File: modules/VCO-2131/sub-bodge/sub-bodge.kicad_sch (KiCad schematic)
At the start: 2 parts

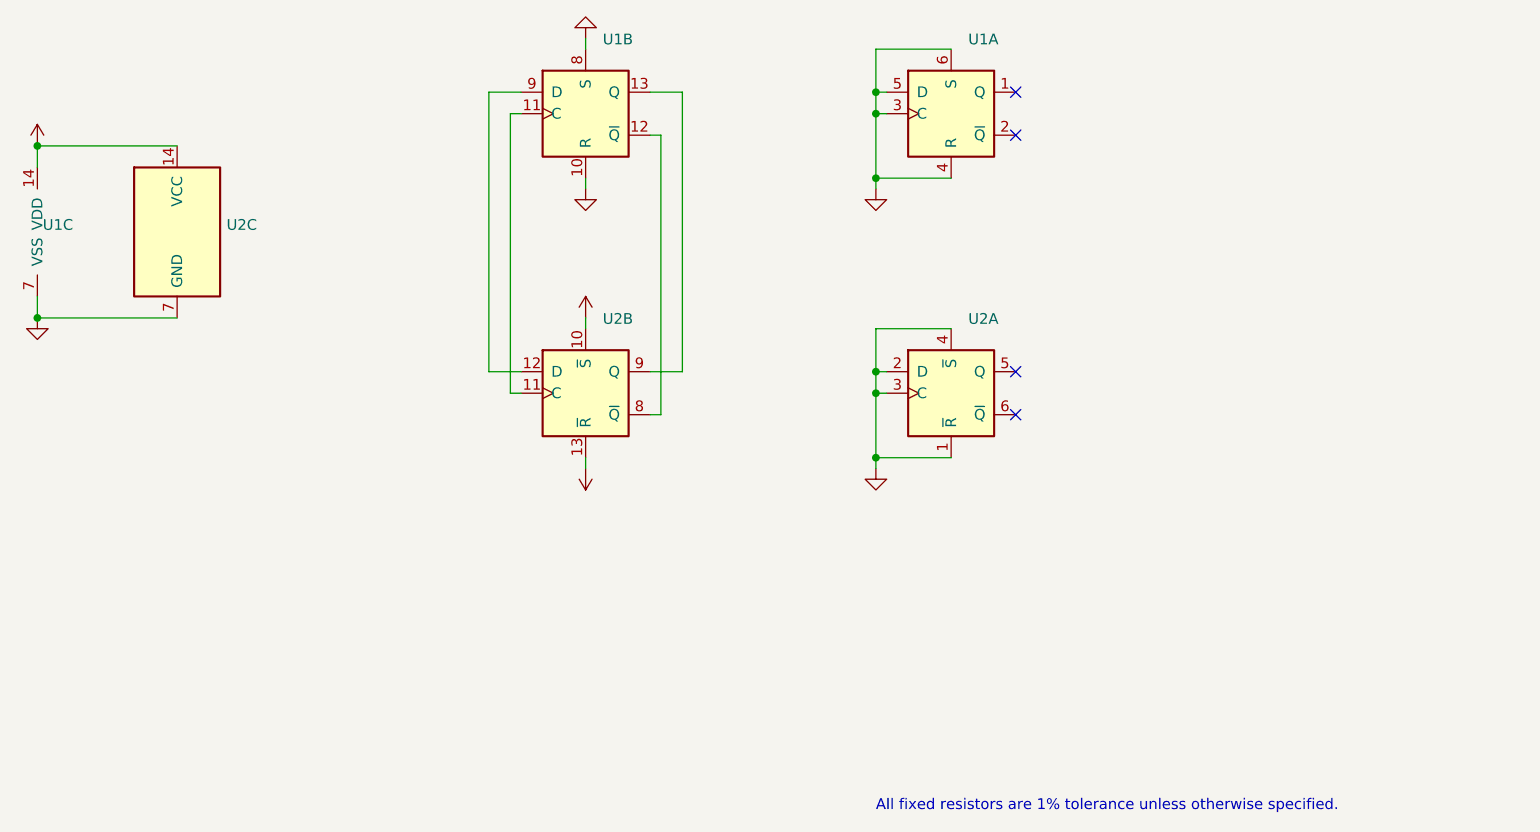
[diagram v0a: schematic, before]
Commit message: VCO sub fix - PCB with SOIC
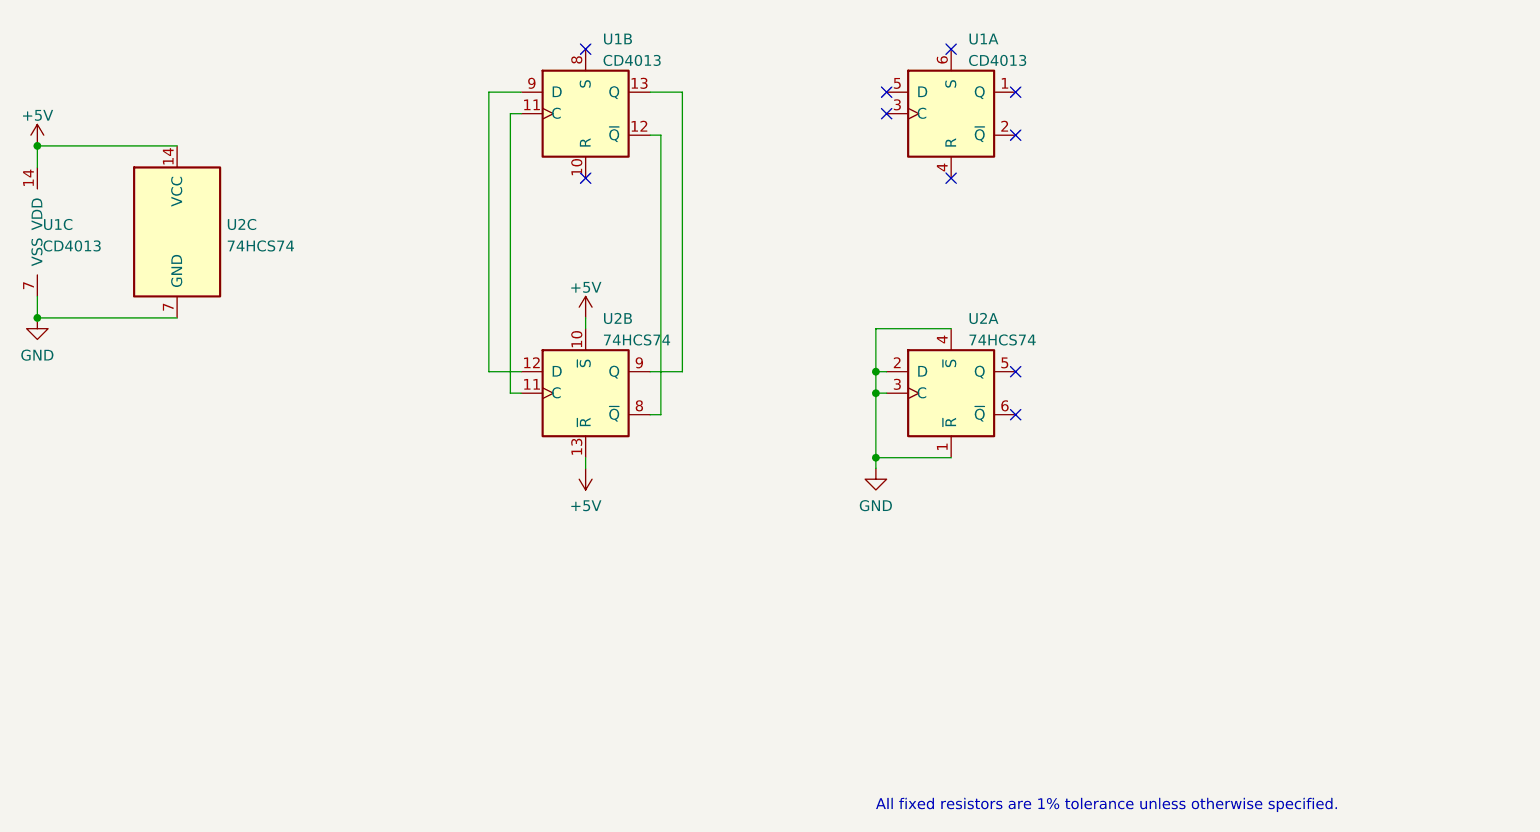
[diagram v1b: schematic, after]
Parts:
- U1: value (none) -> CD4013; footprint (none) -> Package_DIP:DIP-14_W7.62mm
- U2: value (none) -> 74HCS74; footprint (none) -> Package_SO:SOIC-14_3.9x8.7mm_P1.27mm
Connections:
- net GND: no longer U1.10 (R), U1.3 (C), U1.4 (R), U1.5 (D), U1.6 (S), U1.8 (S)
- no-connect marks 4 -> 10

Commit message: VCO sub fix - PCB with SOIC
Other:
- title: [title] -> VCO-2131 Sub Bodge
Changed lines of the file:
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@@
   (paper "A4")
   (title_block
-    (title "[title]")
-    (rev "0.1")
+    (title "VCO-2131 Sub Bodge")
+    (date "2022-07-04")
+    (rev "1.0")
     (company "Len Popp")
     (comment 1 "Copyright © 2022 Len Popp CC BY")
-    (comment 2 "[description]")
+    (comment 2 "Bodge board to fix sub-oscillator")
   )
   (junction (at 177.8 104.14) (diameter 0) (color 0 0 0 0)

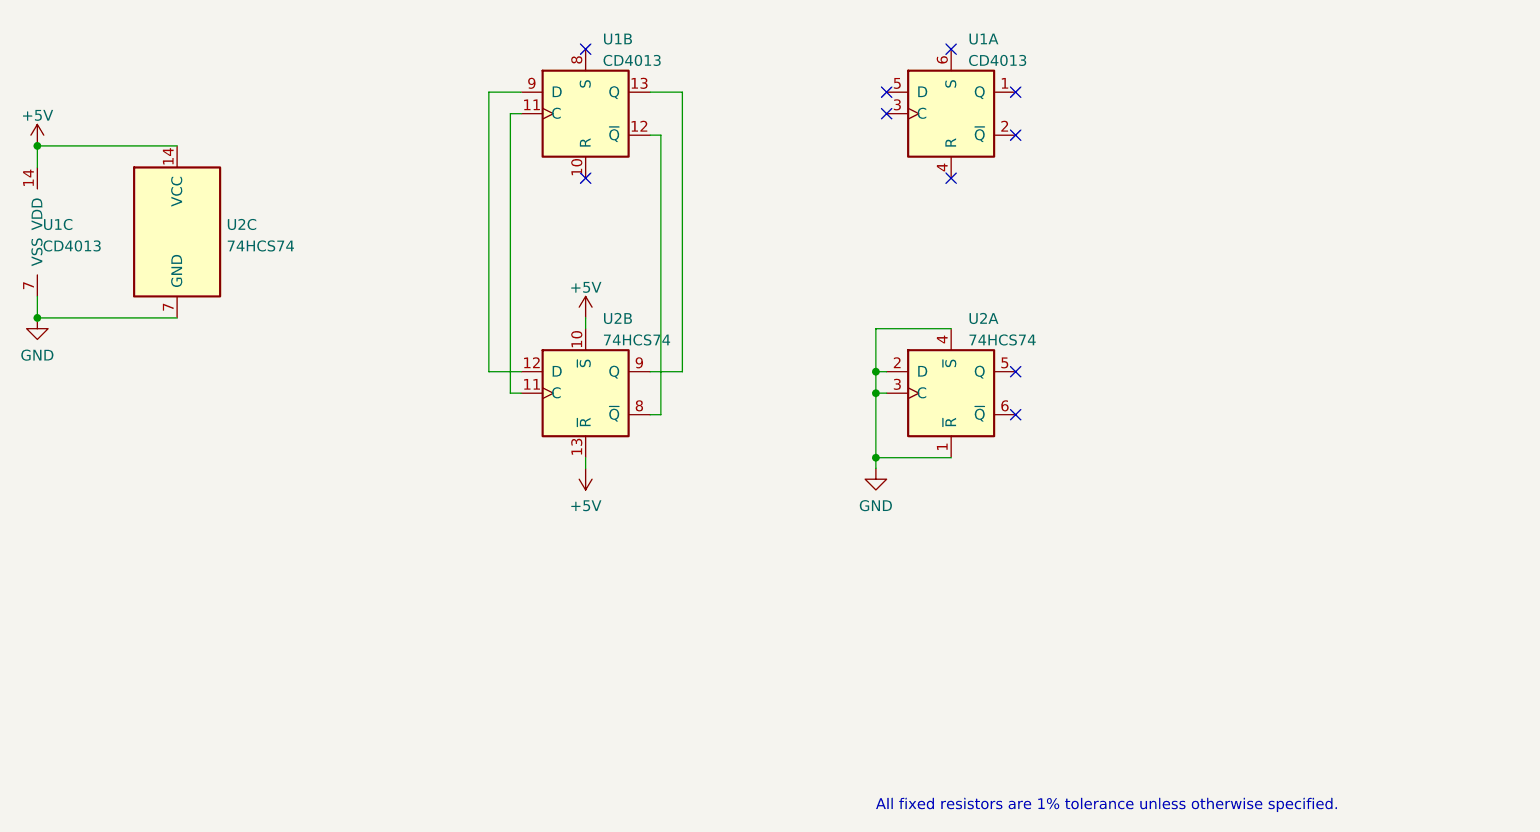
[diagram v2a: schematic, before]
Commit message: VCO sub fix - update component
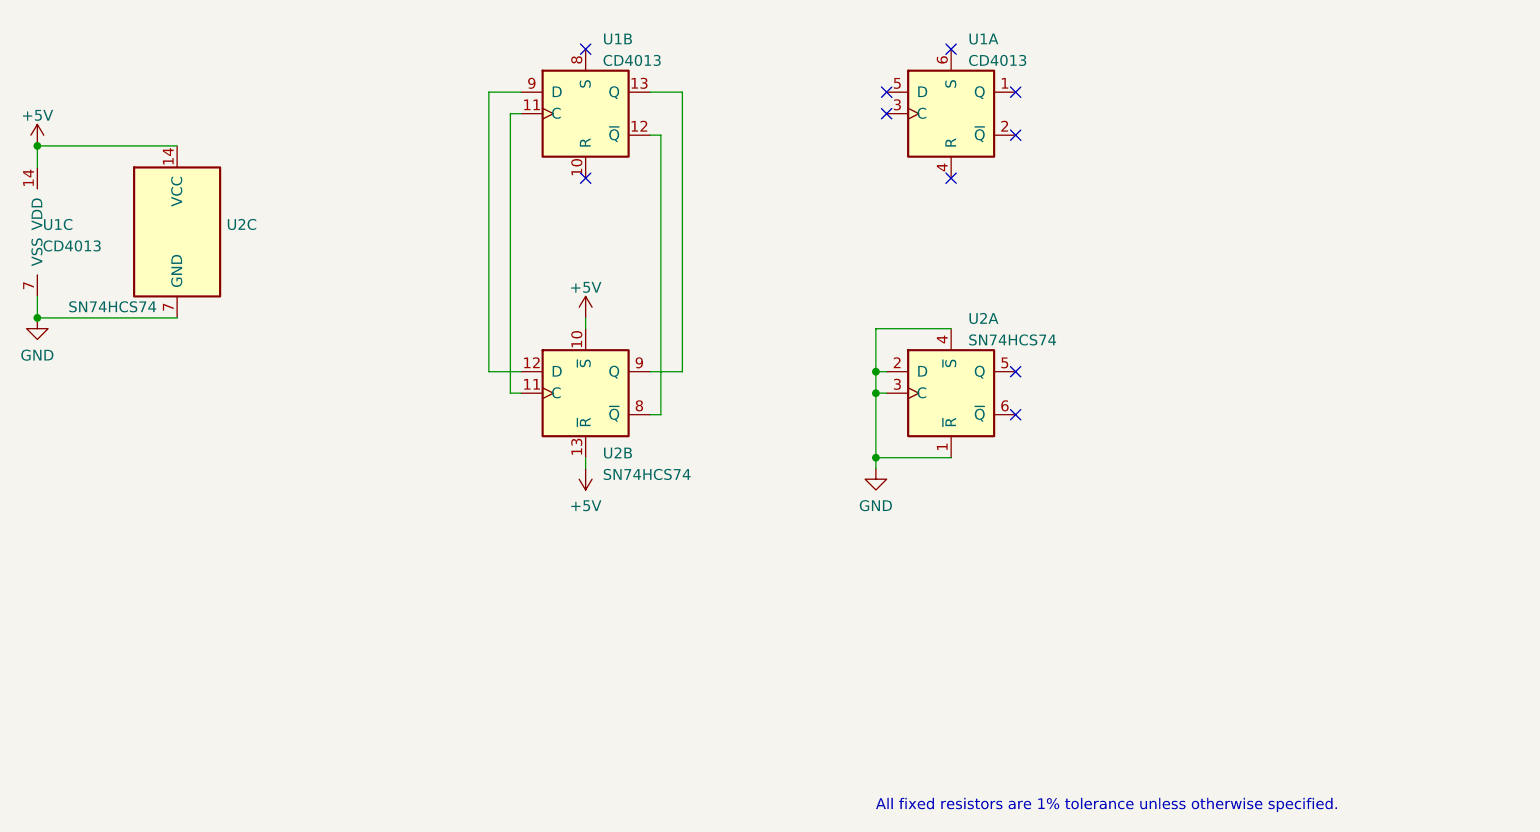
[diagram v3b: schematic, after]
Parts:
- U2: value 74HCS74 -> SN74HCS74; symbol 74xx:74HC74 -> -lmp-IC-misc:SN74HCS74; Distributor (none) -> Mouser; DistributorPartLink (none) -> https://www.mouser.ca/ProductDetail/Texas-Instruments/SN74H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; DistributorPartNum (none) -> 595-SN74HCS74DR; Manufacturer (none) -> Texas Instruments; ManufacturerPartNum (none) -> SN74HCS74DR
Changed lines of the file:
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@@
     (pin "7")
   )
-  (symbol (lib_id "74xx:74HC74") (at 95.25 87.63 0) (unit 3)
+  (symbol (lib_id "-lmp-IC-misc:SN74HCS74") (at 95.25 87.63 0) (unit 3)
     (in_bom yes) (on_board yes) (fields_autoplaced)
     (property "Reference" "U2" (id 0) (at 101.092 86.7953 0)
       (effects (font (size 1.27 1.27)) (justify left))
     )
-    (property "Value" "74HCS74" (id 1) (at 101.092 89.3322 0)
-      (effects (font (size 1.27 1.27)) (justify left))
-    )
+    (property "Value" "SN74HCS74" (id 1) (at 87.63 96.52 0))
     (property "Footprint" "Package_SO:SOIC-14_3.9x8.7mm_P1.27mm" (id 2) (at 95.25 87.63 0)
       (effects (font (size 1.27 1.27)) hide)
     )
     (property "Datasheet" "https://www.ti.com/lit/ds/symlink/sn74hcs74.pdf" (id 3) (at 95.25 87.63 0)
+      (effects (font (size 1.27 1.27)) hide)
+    )
+    (property "Manufacturer" "Texas Instruments" (id 4) (at 95.25 87.63 0)
+      (effects (font (size 1.27 1.27)) hide)
+    )
+    (property "ManufacturerPartNum" "SN74HCS74DR" (id 5) (at 95.25 87.63 0)
+      (effects (font (size 1.27 1.27)) hide)
+    )
+    (property "Distributor" "Mouser" (id 6) (at 95.25 87.63 0)
+      (effects (font (size 1.27 1.27)) hide)
+    )
+    (property "DistributorPartNum" "595-SN74HCS74DR" (id 7) (at 95.25 87.63 0)
+      (effects (font (size 1.27 1.27)) hide)
+    )
+    (property "DistributorPartLink" "https://www.mouser.ca/ProductDetail/Texas-Instruments/SN74HCS74DR?qs=TiOZkKH1s2QvGxo75w4r5Q%3D%3D" (id 8) (at 95.25 87.63 0)
       (effects (font (size 1.27 1.27)) hide)
     )
@@
     (pin "1")
   )
-  (symbol (lib_id "74xx:74HC74") (at 143.51 106.68 0) (unit 2)
-    (in_bom yes) (on_board yes) (fields_autoplaced)
-    (property "Reference" "U2" (id 0) (at 145.5294 97.9002 0)
-      (effects (font (size 1.27 1.27)) (justify left))
-    )
-    (property "Value" "74HCS74" (id 1) (at 145.5294 100.4371 0)
+  (symbol (lib_id "-lmp-IC-misc:SN74HCS74") (at 143.51 106.68 0) (unit 2)
+    (in_bom yes) (on_board yes) (fields_autoplaced)
+    (property "Reference" "U2" (id 0) (at 145.5294 113.7904 0)
+      (effects (font (size 1.27 1.27)) (justify left))
+    )
+    (property "Value" "SN74HCS74" (id 1) (at 145.5294 116.3273 0)
       (effects (font (size 1.27 1.27)) (justify left))
     )
@@
     )
     (property "Datasheet" "https://www.ti.com/lit/ds/symlink/sn74hcs74.pdf" (id 3) (at 143.51 106.68 0)
+      (effects (font (size 1.27 1.27)) hide)
+    )
+    (property "Manufacturer" "Texas Instruments" (id 4) (at 143.51 106.68 0)
+      (effects (font (size 1.27 1.27)) hide)
+    )
+    (property "ManufacturerPartNum" "SN74HCS74DR" (id 5) (at 143.51 106.68 0)
+      (effects (font (size 1.27 1.27)) hide)
+    )
+    (property "Distributor" "Mouser" (id 6) (at 143.51 106.68 0)
+      (effects (font (size 1.27 1.27)) hide)
+    )
+    (property "DistributorPartNum" "595-SN74HCS74DR" (id 7) (at 143.51 106.68 0)
+      (effects (font (size 1.27 1.27)) hide)
+    )
+    (property "DistributorPartLink" "https://www.mouser.ca/ProductDetail/Texas-Instruments/SN74HCS74DR?qs=TiOZkKH1s2QvGxo75w4r5Q%3D%3D" (id 8) (at 143.51 106.68 0)
       (effects (font (size 1.27 1.27)) hide)
     )
@@
     (pin "1")
   )
-  (symbol (lib_id "74xx:74HC74") (at 186.69 106.68 0) (unit 1)
+  (symbol (lib_id "-lmp-IC-misc:SN74HCS74") (at 186.69 106.68 0) (unit 1)
     (in_bom yes) (on_board yes) (fields_autoplaced)
     (property "Reference" "U2" (id 0) (at 188.7094 97.9002 0)
       (effects (font (size 1.27 1.27)) (justify left))
     )
-    (property "Value" "74HCS74" (id 1) (at 188.7094 100.4371 0)
+    (property "Value" "SN74HCS74" (id 1) (at 188.7094 100.4371 0)
       (effects (font (size 1.27 1.27)) (justify left))
     )
@@
     )
     (property "Datasheet" "https://www.ti.com/lit/ds/symlink/sn74hcs74.pdf" (id 3) (at 186.69 106.68 0)
+      (effects (font (size 1.27 1.27)) hide)
+    )
+    (property "Manufacturer" "Texas Instruments" (id 4) (at 186.69 106.68 0)
+      (effects (font (size 1.27 1.27)) hide)
+    )
+    (property "ManufacturerPartNum" "SN74HCS74DR" (id 5) (at 186.69 106.68 0)
+      (effects (font (size 1.27 1.27)) hide)
+    )
+    (property "Distributor" "Mouser" (id 6) (at 186.69 106.68 0)
+      (effects (font (size 1.27 1.27)) hide)
+    )
+    (property "DistributorPartNum" "595-SN74HCS74DR" (id 7) (at 186.69 106.68 0)
+      (effects (font (size 1.27 1.27)) hide)
+    )
+    (property "DistributorPartLink" "https://www.mouser.ca/ProductDetail/Texas-Instruments/SN74HCS74DR?qs=TiOZkKH1s2QvGxo75w4r5Q%3D%3D" (id 8) (at 186.69 106.68 0)
       (effects (font (size 1.27 1.27)) hide)
     )
@@
     )
     (path "/a6b973bf-3c82-4206-bae7-4f835d16d359"
-      (reference "U2") (unit 1) (value "74HCS74") (footprint "Package_SO:SOIC-14_3.9x8.7mm_P1.27mm")
+      (reference "U2") (unit 1) (value "SN74HCS74") (footprint "Package_SO:SOIC-14_3.9x8.7mm_P1.27mm")
     )
     (path "/6d7ff4f8-4e48-4266-a389-7862ef11491b"
-      (reference "U2") (unit 2) (value "74HCS74") (footprint "Package_SO:SOIC-14_3.9x8.7mm_P1.27mm")
+      (reference "U2") (unit 2) (value "SN74HCS74") (footprint "Package_SO:SOIC-14_3.9x8.7mm_P1.27mm")
     )
     (path "/5f25f432-22ee-4e60-9cf8-02b904961add"
-      (reference "U2") (unit 3) (value "74HCS74") (footprint "Package_SO:SOIC-14_3.9x8.7mm_P1.27mm")
-    )
-  )
+      (reference "U2") (unit 3) (value "SN74HCS74") (footprint "Package_SO:SOIC-14_3.9x8.7mm_P1.27mm")
+    )
+  )
